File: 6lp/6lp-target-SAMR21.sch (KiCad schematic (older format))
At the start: 23 parts, among them SW1 SW_PUSH, T1 2450BM15A0015, U3 SAMR21E, X1 CRYSTAL-4

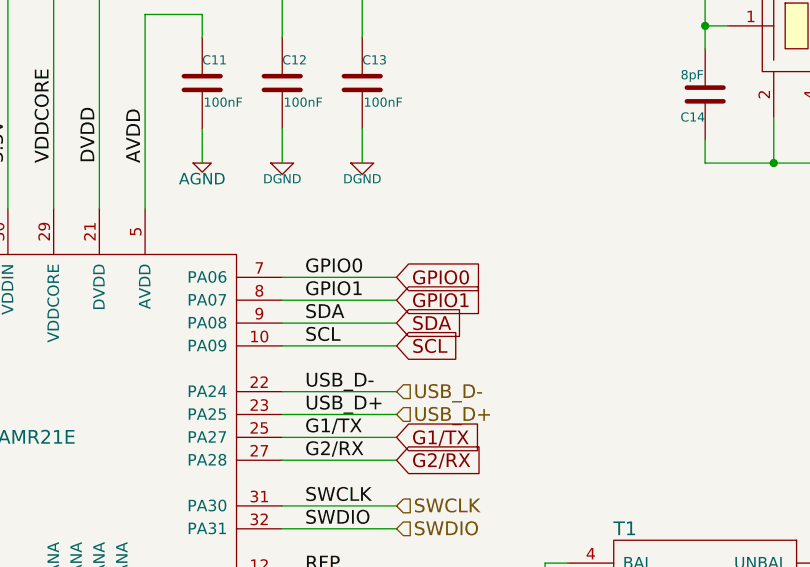
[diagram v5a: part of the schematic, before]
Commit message: layout passes drc
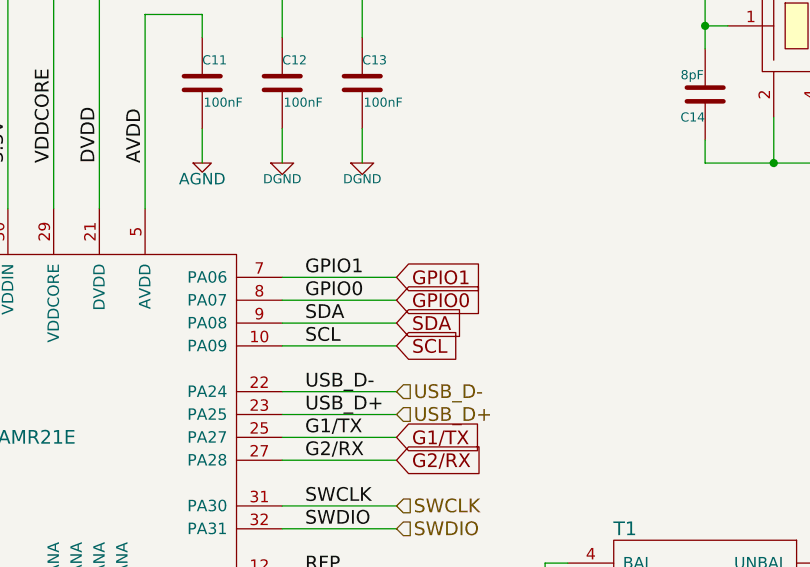
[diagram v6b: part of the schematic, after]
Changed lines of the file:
@@
 $EndDescr
 $Comp
-L AGND #PWR025
+L AGND #PWR37
 U 1 1 5453137E
 P 4650 5750
-F 0 "#PWR025" H 4650 5750 40  0001 C CNN
+F 0 "#PWR37" H 4650 5750 40  0001 C CNN
 F 1 "AGND" H 4650 5680 50  0000 C CNN
 F 2 "" H 4650 5750 60  0000 C CNN
@@
 $EndComp
 $Comp
-L DGND #PWR026
+L DGND #PWR35
 U 1 1 5453138D
 P 4050 5950
-F 0 "#PWR026" H 4050 5950 40  0001 C CNN
+F 0 "#PWR35" H 4050 5950 40  0001 C CNN
 F 1 "DGND" H 4050 5880 40  0000 C CNN
 F 2 "" H 4050 5950 60  0000 C CNN
@@
 $EndComp
 $Comp
-L DGND #PWR027
+L DGND #PWR31
 U 1 1 54531393
 P 2600 3050
-F 0 "#PWR027" H 2600 3050 40  0001 C CNN
+F 0 "#PWR31" H 2600 3050 40  0001 C CNN
 F 1 "DGND" H 2600 2980 40  0000 C CNN
 F 2 "" H 2600 3050 60  0000 C CNN
@@
 $EndComp
 $Comp
-L AGND #PWR028
+L AGND #PWR38
 U 1 1 545313BC
 P 5000 3050
-F 0 "#PWR028" H 5000 3050 40  0001 C CNN
+F 0 "#PWR38" H 5000 3050 40  0001 C CNN
 F 1 "AGND" H 5000 2980 50  0000 C CNN
 F 2 "" H 5000 3050 60  0000 C CNN
@@
 $EndComp
 $Comp
-L DGND #PWR029
+L DGND #PWR28
 U 1 1 545313C2
 P 2250 3050
-F 0 "#PWR029" H 2250 3050 40  0001 C CNN
+F 0 "#PWR28" H 2250 3050 40  0001 C CNN
 F 1 "DGND" H 2250 2980 40  0000 C CNN
 F 2 "" H 2250 3050 60  0000 C CNN
@@
 $EndComp
 $Comp
-L DGND #PWR030
+L DGND #PWR40
 U 1 1 545313C8
 P 5700 3050
-F 0 "#PWR030" H 5700 3050 40  0001 C CNN
+F 0 "#PWR40" H 5700 3050 40  0001 C CNN
 F 1 "DGND" H 5700 2980 40  0000 C CNN
 F 2 "" H 5700 3050 60  0000 C CNN
@@
 $EndComp
 $Comp
-L +3.3V #PWR031
+L +3.3V #PWR27
 U 1 1 545313CE
 P 2250 1650
-F 0 "#PWR031" H 2250 1610 30  0001 C CNN
+F 0 "#PWR27" H 2250 1610 30  0001 C CNN
 F 1 "+3.3V" H 2250 1760 30  0000 C CNN
 F 2 "" H 2250 1650 60  0000 C CNN
@@
 AVDD
 $Comp
-L DGND #PWR032
+L DGND #PWR39
 U 1 1 545313D5
 P 5350 3050
-F 0 "#PWR032" H 5350 3050 40  0001 C CNN
+F 0 "#PWR39" H 5350 3050 40  0001 C CNN
 F 1 "DGND" H 5350 2980 40  0000 C CNN
 F 2 "" H 5350 3050 60  0000 C CNN
@@
 SUPPLIED
 $Comp
-L AGND #PWR033
+L AGND #PWR34
 U 1 1 545313DF
 P 3500 3050
-F 0 "#PWR033" H 3500 3050 40  0001 C CNN
+F 0 "#PWR34" H 3500 3050 40  0001 C CNN
 F 1 "AGND" H 3500 2980 50  0000 C CNN
 F 2 "" H 3500 3050 60  0000 C CNN
@@
 $EndComp
 $Comp
-L AGND #PWR034
+L AGND #PWR32
 U 1 1 545313F5
 P 3150 3050
-F 0 "#PWR034" H 3150 3050 40  0001 C CNN
+F 0 "#PWR32" H 3150 3050 40  0001 C CNN
 F 1 "AGND" H 3150 2980 50  0000 C CNN
 F 2 "" H 3150 3050 60  0000 C CNN
@@
 $EndComp
 $Comp
-L DGND #PWR035
+L DGND #PWR26
 U 1 1 54531403
 P 1900 3050
-F 0 "#PWR035" H 1900 3050 40  0001 C CNN
+F 0 "#PWR26" H 1900 3050 40  0001 C CNN
 F 1 "DGND" H 1900 2980 40  0000 C CNN
 F 2 "" H 1900 3050 60  0000 C CNN
@@
 $EndComp
 $Comp
-L DGND #PWR036
+L DGND #PWR30
 U 1 1 54531418
 P 2550 5650
-F 0 "#PWR036" H 2550 5650 40  0001 C CNN
+F 0 "#PWR30" H 2550 5650 40  0001 C CNN
 F 1 "DGND" H 2550 5580 40  0000 C CNN
 F 2 "" H 2550 5650 60  0000 C CNN
@@
 $EndComp
 $Comp
-L +3.3V #PWR037
+L +3.3V #PWR29
 U 1 1 54531425
 P 2450 4300
-F 0 "#PWR037" H 2450 4260 30  0001 C CNN
+F 0 "#PWR29" H 2450 4260 30  0001 C CNN
 F 1 "+3.3V" H 2450 4410 30  0000 C CNN
 F 2 "" H 2450 4300 60  0000 C CNN
@@
 $EndComp
 $Comp
-L AGND #PWR038
+L AGND #PWR41
 U 1 1 54531457
 P 7100 5650
-F 0 "#PWR038" H 7100 5650 40  0001 C CNN
+F 0 "#PWR41" H 7100 5650 40  0001 C CNN
 F 1 "AGND" H 7100 5580 50  0000 C CNN
 F 2 "" H 7100 5650 60  0000 C CNN
@@
 $EndComp
 $Comp
-L AGND #PWR039
+L AGND #PWR43
 U 1 1 5453145D
 P 9300 5650
-F 0 "#PWR039" H 9300 5650 40  0001 C CNN
+F 0 "#PWR43" H 9300 5650 40  0001 C CNN
 F 1 "AGND" H 9300 5580 50  0000 C CNN
 F 2 "" H 9300 5650 60  0000 C CNN
@@
 $EndComp
 $Comp
-L DGND #PWR040
+L DGND #PWR25
 U 1 1 54531483
 P 1650 5150
-F 0 "#PWR040" H 1650 5150 40  0001 C CNN
+F 0 "#PWR25" H 1650 5150 40  0001 C CNN
 F 1 "DGND" H 1650 5080 40  0000 C CNN
 F 2 "" H 1650 5150 60  0000 C CNN
@@
 $EndComp
 $Comp
-L DGND #PWR041
+L DGND #PWR42
 U 1 1 54532400
 P 8000 3200
-F 0 "#PWR041" H 8000 3200 40  0001 C CNN
+F 0 "#PWR42" H 8000 3200 40  0001 C CNN
 F 1 "DGND" H 8000 3130 40  0000 C CNN
 F 2 "" H 8000 3200 60  0000 C CNN
@@
 RADIO AND DIGITAL\nPOWER DOMAIN BRIDGE
 $Comp
-L AGND #PWR042
+L AGND #PWR33
 U 1 1 54539592
 P 3250 7250
-F 0 "#PWR042" H 3250 7250 40  0001 C CNN
+F 0 "#PWR33" H 3250 7250 40  0001 C CNN
 F 1 "AGND" H 3250 7180 50  0000 C CNN
 F 2 "" H 3250 7250 60  0000 C CNN
@@
 $EndComp
 $Comp
-L DGND #PWR043
+L DGND #PWR36
 U 1 1 54539598
 P 4100 7250
-F 0 "#PWR043" H 4100 7250 40  0001 C CNN
+F 0 "#PWR36" H 4100 7250 40  0001 C CNN
 F 1 "DGND" H 4100 7180 40  0000 C CNN
 F 2 "" H 4100 7250 60  0000 C CNN
@@
 Text Label 9300 4000 0    60   ~ 0
 GPIO3
+Text Label 5450 3650 0    60   ~ 0
+GPIO0
 Text Label 5450 3550 0    60   ~ 0
-GPIO0
-Text Label 5450 3650 0    60   ~ 0
 GPIO1
 Text Label 3150 3550 2    60   ~ 0
@@
 Text Label 3150 3650 2    60   ~ 0
 GPIO3
+Text GLabel 5850 3650 2    60   Input ~ 0
+GPIO0
 Text GLabel 5850 3550 2    60   Input ~ 0
-GPIO0
-Text GLabel 5850 3650 2    60   Input ~ 0
 GPIO1
 Text GLabel 2800 3550 0    60   Input ~ 0

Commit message: changes w/ schem, layout review. passes drc.
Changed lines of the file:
@@
 $EndDescr
 $Comp
-L AGND #PWR37
+L AGND #PWR025
 U 1 1 5453137E
 P 4650 5750
-F 0 "#PWR37" H 4650 5750 40  0001 C CNN
+F 0 "#PWR025" H 4650 5750 40  0001 C CNN
 F 1 "AGND" H 4650 5680 50  0000 C CNN
 F 2 "" H 4650 5750 60  0000 C CNN
@@
 $EndComp
 $Comp
-L DGND #PWR35
+L DGND #PWR026
 U 1 1 5453138D
 P 4050 5950
-F 0 "#PWR35" H 4050 5950 40  0001 C CNN
+F 0 "#PWR026" H 4050 5950 40  0001 C CNN
 F 1 "DGND" H 4050 5880 40  0000 C CNN
 F 2 "" H 4050 5950 60  0000 C CNN
@@
 $EndComp
 $Comp
-L DGND #PWR31
+L DGND #PWR027
 U 1 1 54531393
 P 2600 3050
-F 0 "#PWR31" H 2600 3050 40  0001 C CNN
+F 0 "#PWR027" H 2600 3050 40  0001 C CNN
 F 1 "DGND" H 2600 2980 40  0000 C CNN
 F 2 "" H 2600 3050 60  0000 C CNN
@@
 $EndComp
 $Comp
-L AGND #PWR38
+L AGND #PWR028
 U 1 1 545313BC
 P 5000 3050
-F 0 "#PWR38" H 5000 3050 40  0001 C CNN
+F 0 "#PWR028" H 5000 3050 40  0001 C CNN
 F 1 "AGND" H 5000 2980 50  0000 C CNN
 F 2 "" H 5000 3050 60  0000 C CNN
@@
 $EndComp
 $Comp
-L DGND #PWR28
+L DGND #PWR029
 U 1 1 545313C2
 P 2250 3050
-F 0 "#PWR28" H 2250 3050 40  0001 C CNN
+F 0 "#PWR029" H 2250 3050 40  0001 C CNN
 F 1 "DGND" H 2250 2980 40  0000 C CNN
 F 2 "" H 2250 3050 60  0000 C CNN
@@
 $EndComp
 $Comp
-L DGND #PWR40
+L DGND #PWR030
 U 1 1 545313C8
 P 5700 3050
-F 0 "#PWR40" H 5700 3050 40  0001 C CNN
+F 0 "#PWR030" H 5700 3050 40  0001 C CNN
 F 1 "DGND" H 5700 2980 40  0000 C CNN
 F 2 "" H 5700 3050 60  0000 C CNN
@@
 $EndComp
 $Comp
-L +3.3V #PWR27
+L +3.3V #PWR031
 U 1 1 545313CE
 P 2250 1650
-F 0 "#PWR27" H 2250 1610 30  0001 C CNN
+F 0 "#PWR031" H 2250 1610 30  0001 C CNN
 F 1 "+3.3V" H 2250 1760 30  0000 C CNN
 F 2 "" H 2250 1650 60  0000 C CNN
@@
 AVDD
 $Comp
-L DGND #PWR39
+L DGND #PWR032
 U 1 1 545313D5
 P 5350 3050
-F 0 "#PWR39" H 5350 3050 40  0001 C CNN
+F 0 "#PWR032" H 5350 3050 40  0001 C CNN
 F 1 "DGND" H 5350 2980 40  0000 C CNN
 F 2 "" H 5350 3050 60  0000 C CNN
@@
 SUPPLIED
 $Comp
-L AGND #PWR34
+L AGND #PWR033
 U 1 1 545313DF
 P 3500 3050
-F 0 "#PWR34" H 3500 3050 40  0001 C CNN
+F 0 "#PWR033" H 3500 3050 40  0001 C CNN
 F 1 "AGND" H 3500 2980 50  0000 C CNN
 F 2 "" H 3500 3050 60  0000 C CNN
@@
 $EndComp
 $Comp
-L AGND #PWR32
+L AGND #PWR034
 U 1 1 545313F5
 P 3150 3050
-F 0 "#PWR32" H 3150 3050 40  0001 C CNN
+F 0 "#PWR034" H 3150 3050 40  0001 C CNN
 F 1 "AGND" H 3150 2980 50  0000 C CNN
 F 2 "" H 3150 3050 60  0000 C CNN
@@
 $EndComp
 $Comp
-L DGND #PWR26
+L DGND #PWR035
 U 1 1 54531403
 P 1900 3050
-F 0 "#PWR26" H 1900 3050 40  0001 C CNN
+F 0 "#PWR035" H 1900 3050 40  0001 C CNN
 F 1 "DGND" H 1900 2980 40  0000 C CNN
 F 2 "" H 1900 3050 60  0000 C CNN
@@
 $EndComp
 $Comp
-L DGND #PWR30
+L DGND #PWR036
 U 1 1 54531418
 P 2550 5650
-F 0 "#PWR30" H 2550 5650 40  0001 C CNN
+F 0 "#PWR036" H 2550 5650 40  0001 C CNN
 F 1 "DGND" H 2550 5580 40  0000 C CNN
 F 2 "" H 2550 5650 60  0000 C CNN
@@
 $EndComp
 $Comp
-L +3.3V #PWR29
+L +3.3V #PWR037
 U 1 1 54531425
 P 2450 4300
-F 0 "#PWR29" H 2450 4260 30  0001 C CNN
+F 0 "#PWR037" H 2450 4260 30  0001 C CNN
 F 1 "+3.3V" H 2450 4410 30  0000 C CNN
 F 2 "" H 2450 4300 60  0000 C CNN
@@
 $EndComp
 $Comp
-L AGND #PWR41
+L AGND #PWR038
 U 1 1 54531457
 P 7100 5650
-F 0 "#PWR41" H 7100 5650 40  0001 C CNN
+F 0 "#PWR038" H 7100 5650 40  0001 C CNN
 F 1 "AGND" H 7100 5580 50  0000 C CNN
 F 2 "" H 7100 5650 60  0000 C CNN
@@
 $EndComp
 $Comp
-L AGND #PWR43
+L AGND #PWR039
 U 1 1 5453145D
 P 9300 5650
-F 0 "#PWR43" H 9300 5650 40  0001 C CNN
+F 0 "#PWR039" H 9300 5650 40  0001 C CNN
 F 1 "AGND" H 9300 5580 50  0000 C CNN
 F 2 "" H 9300 5650 60  0000 C CNN
@@
 $EndComp
 $Comp
-L DGND #PWR25
+L DGND #PWR040
 U 1 1 54531483
 P 1650 5150
-F 0 "#PWR25" H 1650 5150 40  0001 C CNN
+F 0 "#PWR040" H 1650 5150 40  0001 C CNN
 F 1 "DGND" H 1650 5080 40  0000 C CNN
 F 2 "" H 1650 5150 60  0000 C CNN
@@
 $EndComp
 $Comp
-L DGND #PWR42
+L DGND #PWR041
 U 1 1 54532400
 P 8000 3200
-F 0 "#PWR42" H 8000 3200 40  0001 C CNN
+F 0 "#PWR041" H 8000 3200 40  0001 C CNN
 F 1 "DGND" H 8000 3130 40  0000 C CNN
 F 2 "" H 8000 3200 60  0000 C CNN
@@
 Wire Wire Line
 	7200 2950 7200 3050
-Text Notes 3200 6900 0    60   ~ 0
+Text Notes 3150 6900 0    60   ~ 0
 RADIO AND DIGITAL\nPOWER DOMAIN BRIDGE
 $Comp
-L AGND #PWR33
+L AGND #PWR042
 U 1 1 54539592
-P 3250 7250
-F 0 "#PWR33" H 3250 7250 40  0001 C CNN
-F 1 "AGND" H 3250 7180 50  0000 C CNN
-F 2 "" H 3250 7250 60  0000 C CNN
-F 3 "" H 3250 7250 60  0000 C CNN
-	1    3250 7250
+P 3200 7250
+F 0 "#PWR042" H 3200 7250 40  0001 C CNN
+F 1 "AGND" H 3200 7180 50  0000 C CNN
+F 2 "" H 3200 7250 60  0000 C CNN
+F 3 "" H 3200 7250 60  0000 C CNN
+	1    3200 7250
 	-1   0    0    -1
 $EndComp
 $Comp
-L DGND #PWR36
+L DGND #PWR043
 U 1 1 54539598
 P 4100 7250
-F 0 "#PWR36" H 4100 7250 40  0001 C CNN
+F 0 "#PWR043" H 4100 7250 40  0001 C CNN
 F 1 "DGND" H 4100 7180 40  0000 C CNN
 F 2 "" H 4100 7250 60  0000 C CNN
@@
 $EndComp
 Wire Wire Line
-	3250 7150 3250 7250
-Wire Wire Line
-	3250 7150 3350 7150
+	3200 7150 3200 7250
+Wire Wire Line
+	3200 7150 3350 7150
 Wire Wire Line
 	3950 7150 4100 7150

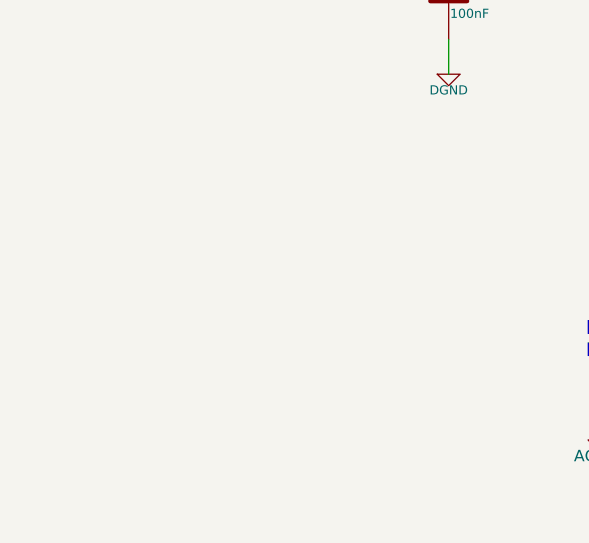
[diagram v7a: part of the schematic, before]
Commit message: power select circuitry
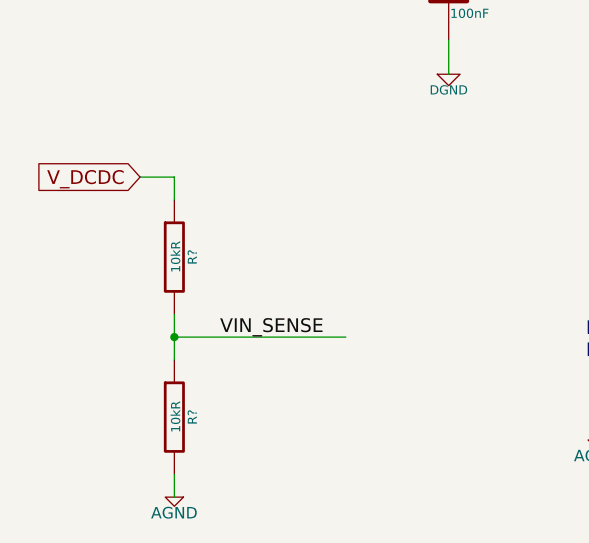
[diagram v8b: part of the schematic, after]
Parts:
- added R? (x2): 10kR, parts:SMD-0402, symbol R
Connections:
- net labels added: VIN_SENSE, V_DCDC
- wire segments 115 -> 120
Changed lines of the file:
@@
 EESchema Schematic File Version 2
-LIBS:74xgxx
-LIBS:74xx
-LIBS:ac-dc
-LIBS:actel
-LIBS:adc-dac
-LIBS:analog_switches
-LIBS:atmel
-LIBS:audio
-LIBS:brooktre
-LIBS:cmos4000
-LIBS:cmos_ieee
-LIBS:conn
-LIBS:contrib
-LIBS:cypress
-LIBS:dc-dc
-LIBS:device
-LIBS:digital-audio
-LIBS:display
-LIBS:dsp
-LIBS:elec-unifil
-LIBS:ftdi
-LIBS:gennum
-LIBS:graphic
-LIBS:hc11
-LIBS:intel
-LIBS:interface
-LIBS:ir
-LIBS:linear
-LIBS:logo
-LIBS:memory
-LIBS:microchip
-LIBS:microchip1
-LIBS:microchip_pic10mcu
-LIBS:microchip_pic12mcu
-LIBS:microchip_pic16mcu
-LIBS:microchip_pic18mcu
-LIBS:microcontrollers
-LIBS:motorola
-LIBS:msp430
-LIBS:nxp_armmcu
-LIBS:opto
-LIBS:philips
 LIBS:power
-LIBS:powerint
-LIBS:pspice
-LIBS:references
-LIBS:regul
-LIBS:relays
-LIBS:rfcom
-LIBS:sensors
-LIBS:siliconi
-LIBS:special
-LIBS:stm8
-LIBS:stm32
-LIBS:supertex
-LIBS:texas
-LIBS:transf
-LIBS:transistors
-LIBS:ttl_ieee
-LIBS:valves
-LIBS:video
-LIBS:xilinx
-LIBS:parts
 LIBS:6lp-cache
 EELAYER 24 0
@@
 Text GLabel 2800 3750 0    60   Input ~ 0
 MOSI
+Text GLabel 1200 6100 0    60   Input ~ 0
+V_DCDC
+$Comp
+L R R?
+U 1 1 54540406
+P 1350 6450
+F 0 "R?" V 1430 6450 40  0000 C CNN
+F 1 "10kR" V 1357 6451 40  0000 C CNN
+F 2 "parts:SMD-0402" V 1280 6450 30  0001 C CNN
+F 3 "" H 1350 6450 30  0000 C CNN
+	1    1350 6450
+	1    0    0    -1
+$EndComp
+$Comp
+L R R?
+U 1 1 54541C36
+P 1350 7150
+F 0 "R?" V 1430 7150 40  0000 C CNN
+F 1 "10kR" V 1357 7151 40  0000 C CNN
+F 2 "parts:SMD-0402" V 1280 7150 30  0001 C CNN
+F 3 "" H 1350 7150 30  0000 C CNN
+	1    1350 7150
+	1    0    0    -1
+$EndComp
+$Comp
+L AGND #PWR?
+U 1 1 54541CB9
+P 1350 7500
+F 0 "#PWR?" H 1350 7500 40  0001 C CNN
+F 1 "AGND" H 1350 7430 50  0000 C CNN
+F 2 "" H 1350 7500 60  0000 C CNN
+F 3 "" H 1350 7500 60  0000 C CNN
+	1    1350 7500
+	-1   0    0    -1
+$EndComp
+Wire Wire Line
+	1350 7500 1350 7400
+Wire Wire Line
+	1350 6700 1350 6900
+Wire Wire Line
+	1200 6100 1350 6100
+Wire Wire Line
+	1350 6100 1350 6200
+Wire Wire Line
+	1350 6800 2100 6800
+Connection ~ 1350 6800
+Text Label 1550 6800 0    60   ~ 0
+VIN_SENSE
 $EndSCHEMATC
